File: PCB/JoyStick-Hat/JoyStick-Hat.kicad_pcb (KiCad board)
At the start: 4 copper layers, 65 x 120 mm, 88 parts, among them J1 20021121-00010C4LF, J14 Conn_01x03_Pin, J15 Conn_01x03_Pin, J16 Conn_01x06, J2 BU2032SM-JJ-GTR, J3 Conn_02x05_Odd_Even, J4 Conn_02x04_Odd_Even, J6 1757242, J7 Raspberry_Pi_2_3, J8 Conn_01x04_Pin, J9 Conn_01x04_Pin, M1 D24V22F12, M2 D24V22F5, M3 D24V22F3, SW1 TL3301NF260QG, U1 STM32F446VETx, U4 MAX3535ECWI+T, X1 ABM3B-8.000MHZ-B2-T, X2 ABS07-32.768KHZ-9-T

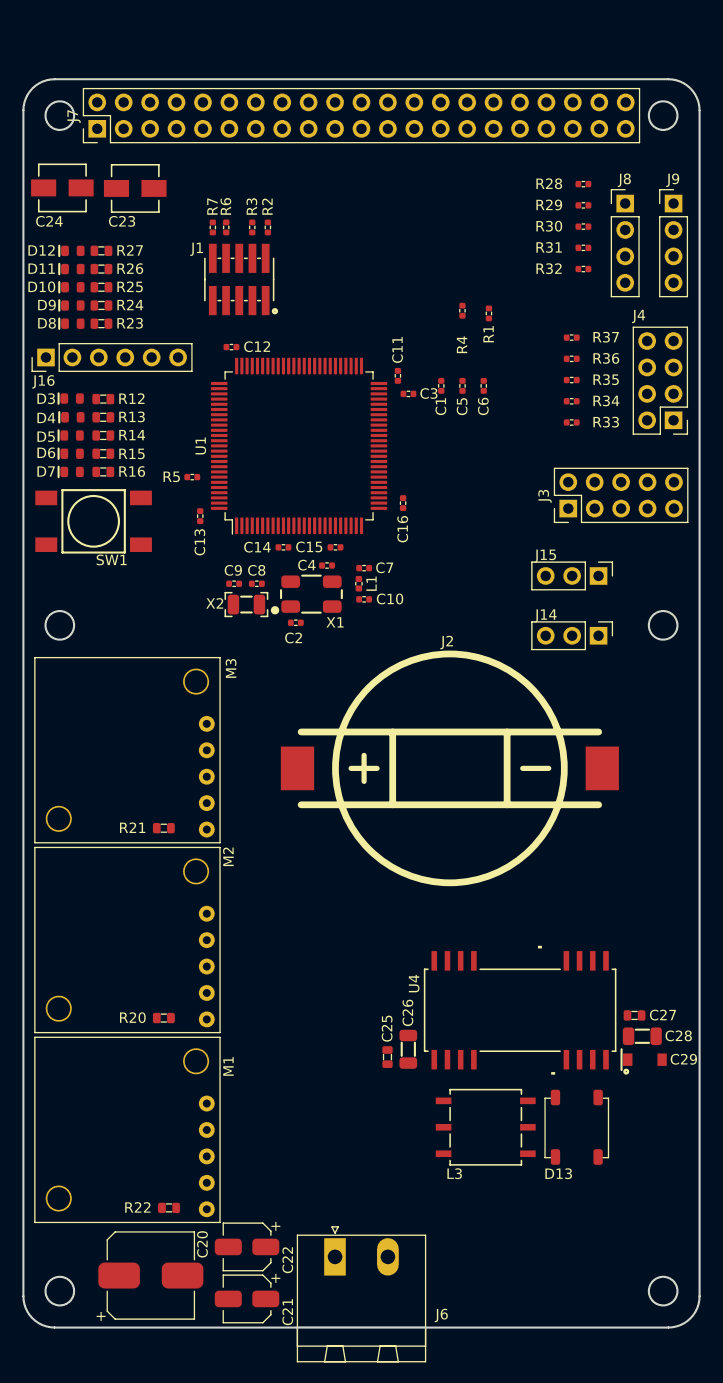
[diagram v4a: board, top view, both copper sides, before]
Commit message: Board Routing
Connectors swapped around and board route started
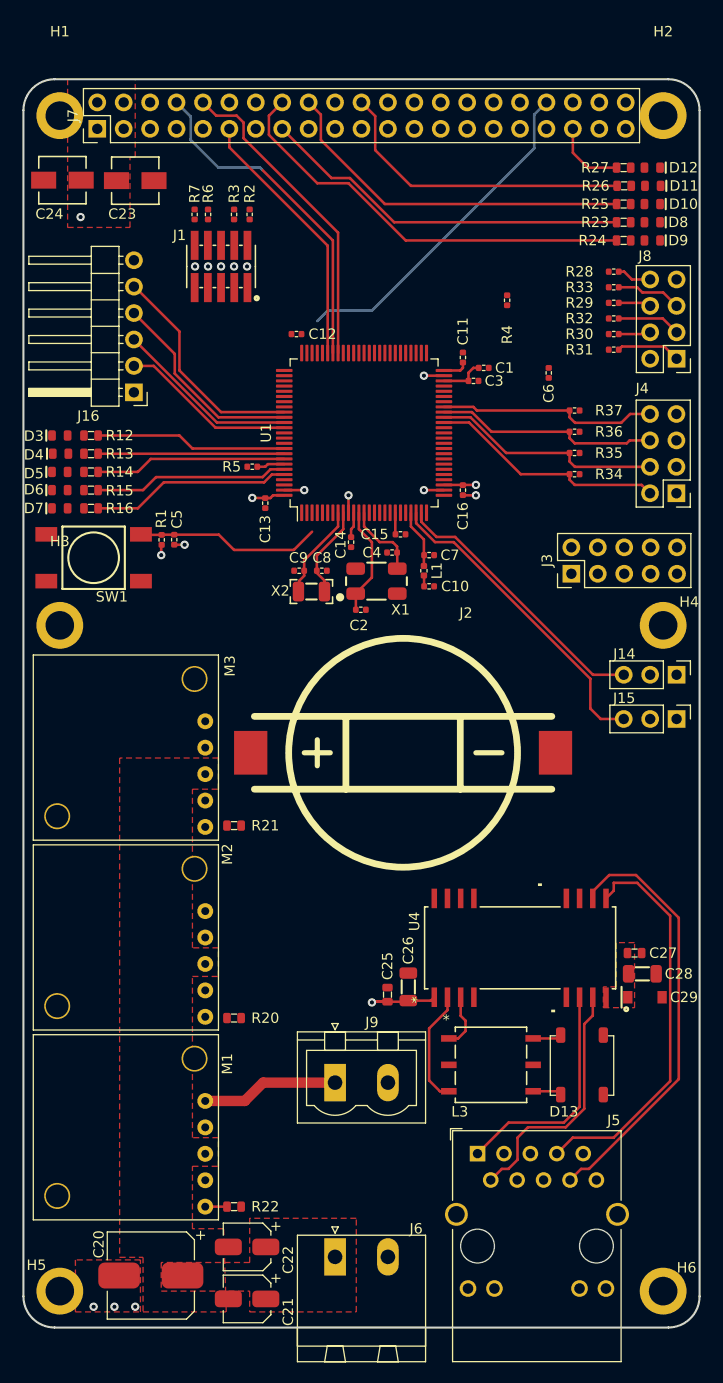
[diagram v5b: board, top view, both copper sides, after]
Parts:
- added H1: MountingHole_Pad, AVR-KiCAD-Lib-Holes_Fasteners:RPI_HAT_HOLE, F.Cu at (203.5, 43.0)
- added H2: MountingHole_Pad, AVR-KiCAD-Lib-Holes_Fasteners:RPI_HAT_HOLE, F.Cu at (261.5, 43.0)
- added H3: MountingHole_Pad, AVR-KiCAD-Lib-Holes_Fasteners:RPI_HAT_HOLE, F.Cu at (203.5, 92.0)
- added H4: MountingHole_Pad, AVR-KiCAD-Lib-Holes_Fasteners:RPI_HAT_HOLE, F.Cu at (261.5, 92.0)
- added H5: MountingHole_Pad, AVR-KiCAD-Lib-Holes_Fasteners:RPI_HAT_HOLE, F.Cu at (203.5, 156.0)
- added H6: MountingHole_Pad, AVR-KiCAD-Lib-Holes_Fasteners:RPI_HAT_HOLE, F.Cu at (261.5, 156.0)
- added J5: 8P8C_LED_Shielded, AVR-KiCAD-Lib-Connectors:RJ45_Wuerth_7499111446_Horizontal, F.Cu at (243.7, 142.8)
- J16: footprint Connector_PinHeader_2.54mm:PinHeader_1x06_P2.54mm_Vertical -> Connector_PinHeader_2.54mm:PinHeader_1x06_P2.54mm_Horizontal
- J8: value Conn_01x04_Pin -> Conn_02x04_Odd_Even; footprint Connector_PinHeader_2.54mm:PinHeader_1x04_P2.54mm_Vertical -> Connector_PinHeader_2.54mm:PinHeader_2x04_P2.54mm_Vertical
- J9: value Conn_01x04_Pin -> 1755736; footprint Connector_PinHeader_2.54mm:PinHeader_1x04_P2.54mm_Vertical -> AVR-KiCAD-Lib-Connectors:PhoenixContact_MSTBVA-G_02x5.08mm_Vertical
- moved J9 90.6 mm to (230.0, 136.0)
- moved D8 56.5 mm to (260.4, 53.2), turned to 0 degrees
- moved D11 56.3 mm to (260.5, 49.8), turned to 0 degrees
- moved D10 56.3 mm to (260.4, 51.5), turned to 0 degrees
- moved D12 56.3 mm to (260.4, 48.0), turned to 0 degrees
- moved D9 56.0 mm to (260.4, 55.0), turned to 0 degrees
- moved R23 51.1 mm to (257.7, 53.2), turned to 180 degrees
- moved R26 50.9 mm to (257.8, 49.8), turned to 180 degrees
- moved R25 50.8 mm to (257.7, 51.5), turned to 180 degrees
- moved R27 50.8 mm to (257.7, 48.0), turned to 180 degrees
- moved R24 50.6 mm to (257.7, 55.0)
- moved R1 38.3 mm to (213.3, 83.8)
- moved C5 31.4 mm to (214.5, 83.8), turned to -90 degrees
- moved J8 15.7 mm to (262.8, 66.4), turned to 180 degrees
- moved J15 15.7 mm to (262.8, 101.0)
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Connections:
- D3 pad 2: unconnected-(D3-Pad2) -> GND
- D4 pad 2: unconnected-(D4-Pad2) -> GND
- D5 pad 2: unconnected-(D5-Pad2) -> GND
- D6 pad 2: unconnected-(D6-Pad2) -> GND
- D7 pad 2: unconnected-(D7-Pad2) -> GND
- J8 pad 2: /JoyStick Interface/ROTARY1_POLE2 -> GND
- J8 pad 3: /JoyStick Interface/ROTARY1_POLE3 -> /JoyStick Interface/ROTARY1_POLE2
- J8 pad 4: GND -> /JoyStick Interface/ROTARY2_POLE3
- J9 pad 1: /JoyStick Interface/ROTARY2_POLE1 -> +12V
- J9 pad 2: /JoyStick Interface/ROTARY2_POLE2 -> GND
- U1 pad 84: Net-(J16-Pin_2) -> Net-(J16-Pin_5)
- U1 pad 85: Net-(J16-Pin_3) -> Net-(J16-Pin_4)
- U1 pad 86: Net-(J16-Pin_4) -> Net-(J16-Pin_3)
- U1 pad 87: Net-(J16-Pin_5) -> Net-(J16-Pin_2)
- U4 pad 12: unconnected-(U4-Z-Pad12) -> Net-(U4-Z)
- U4 pad 13: unconnected-(U4-Y-Pad13) -> Net-(U4-Y)
- U4 pad 15: unconnected-(U4-B-Pad15) -> Net-(U4-B)
- U4 pad 16: unconnected-(U4-A-Pad16) -> Net-(U4-A)
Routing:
- net (no net): track 0.00 -> 355.4 mm
- net +5V: track 0.00 -> 73.8 mm, vias 0 -> 1
- net Net-(U4-A): track 0.00 -> 41.3 mm
- net Net-(J7-GPIO23): track 0.00 -> 41.3 mm
- net Net-(U4-B): track 0.00 -> 38.2 mm
- net Net-(J7-GPIO22): track 0.00 -> 35.9 mm
- net Net-(J7-GPIO24): track 0.00 -> 35.1 mm
- net /RPi_Interface/RPI_ST_UART_TX: track 0.00 -> 32.7 mm
- net /RPi_Interface/RPI_ST_UART_CTS: track 0.00 -> 32.6 mm
- net /RPi_Interface/RPI_ST_UART_RX: track 0.00 -> 30.6 mm
- net /JoyStick Interface/JOYSTICK_Y: track 0.00 -> 30.4 mm
- net Net-(J7-GPIO25): track 0.00 -> 29.8 mm
- net /JoyStick Interface/JOYSTICK_X: track 0.00 -> 26.4 mm
- net /RPi_Interface/RPI_ST_UART_RTS: track 0.00 -> 25.5 mm
- net Net-(U4-Y): track 0.00 -> 24.1 mm
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- added copper zone on F.Cu, net +24V
- added copper zone on In2.Cu, net +3.3V
- added copper zone on F.Cu, net +5V
- added copper zone on F.Cu, net GND
- added copper zone on In1.Cu, net GND
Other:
- outline, holes or cut-outs redrawn

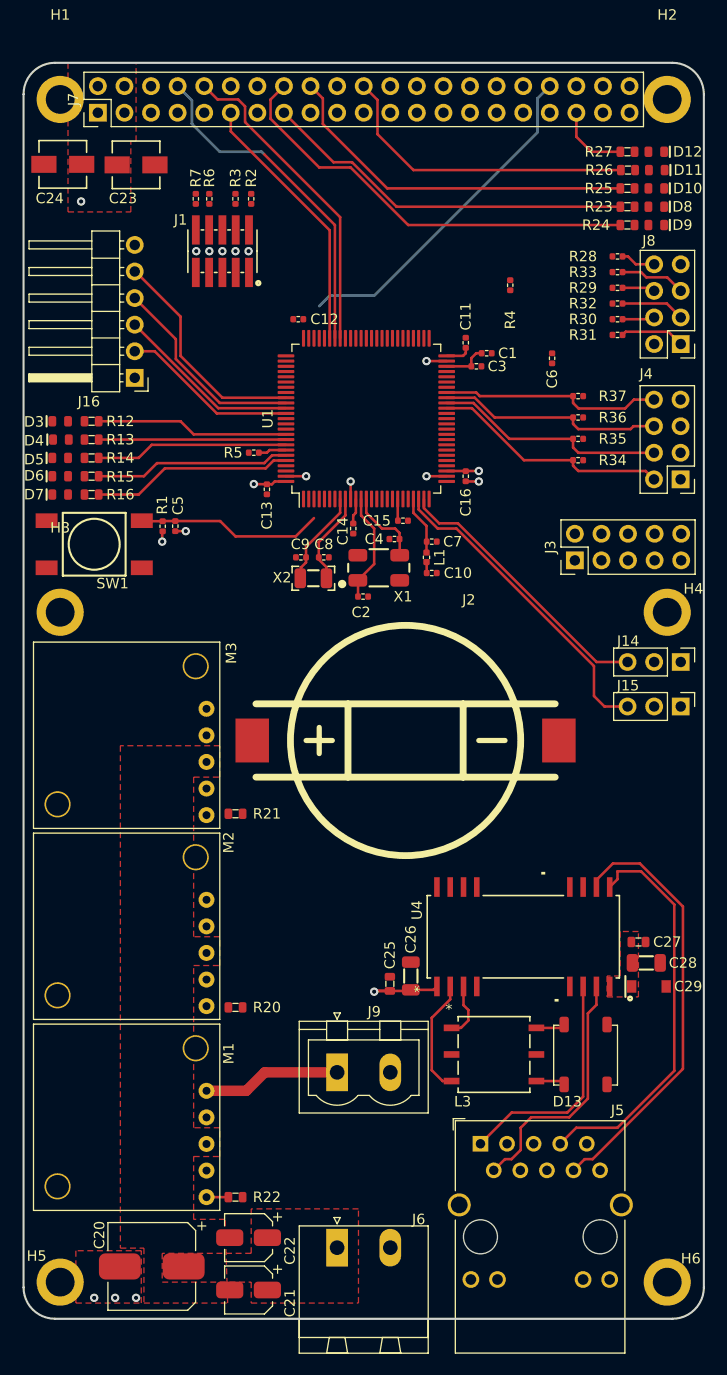
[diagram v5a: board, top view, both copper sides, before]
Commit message: Board Progress
Board route nearly complete, internal power plane topologys witched up to run 5Vs as plane. Reset buttom moved. Next: add more LEDs and breakout more STM32 pins for development purposes.
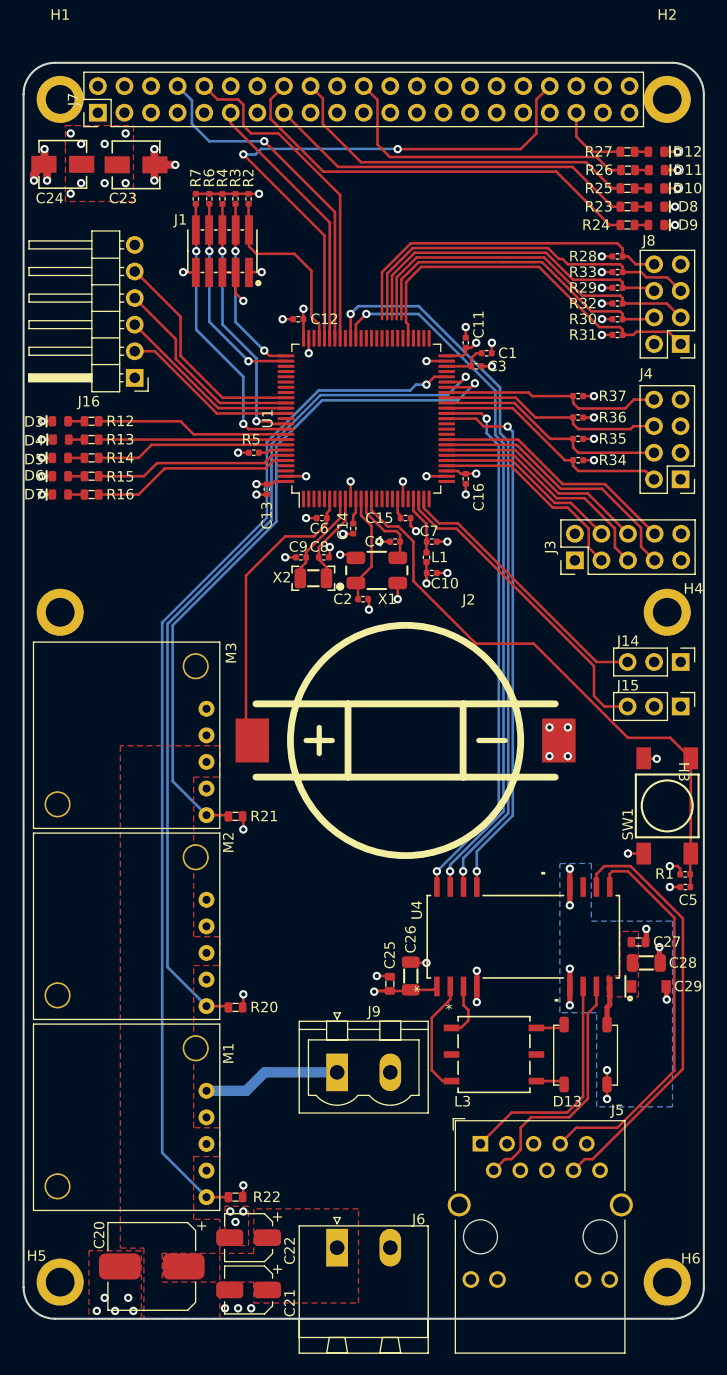
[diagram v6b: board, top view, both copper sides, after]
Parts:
- moved SW1 60.2 mm to (261.5, 110.5), turned to -90 degrees
- moved R1 60.0 mm to (263.2, 117.0), turned to 0 degrees
- moved C5 59.7 mm to (263.2, 118.2), turned to 180 degrees
- moved R4 28.7 mm to (219.0, 52.5), turned to -90 degrees
- moved C6 26.8 mm to (228.5, 83.0), turned to 180 degrees
- moved C15 0.35 mm to (236.5, 83.0)
- moved X1 0.31 mm to (233.8, 88.0)
- moved C4 0.26 mm to (235.5, 85.2)
- moved C16 0.25 mm to (242.2, 79.2)
- moved C2 0.25 mm to (232.4, 90.8)
- moved R2 0.25 mm to (221.5, 52.5)
- moved R21 0.25 mm to (220.2, 111.5), turned to 0 degrees
- turned R20 to 0 degrees
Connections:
- C10 pad 1: +3V3 -> +3.3V
- C11 pad 1: +3V3 -> +3.3V
- C12 pad 1: +3V3 -> +3.3V
- C13 pad 1: +3V3 -> +3.3V
- C14 pad 1: +3V3 -> +3.3V
- C15 pad 1: +3V3 -> +3.3V
- C16 pad 1: +3V3 -> +3.3V
- J1 pad 1: +3V3 -> +3.3V
- J3 pad 1: +3V3 -> +3.3V
- J3 pad 2: +3V3 -> +3.3V
- J3 pad 3: /STM32F446RET6-MCU/LED_DRIVER_SCLK -> /STM32F446RET6-MCU/LED_DRIVER_XLAT
- J3 pad 4: /STM32F446RET6-MCU/LED_DRIVER_XLAT -> /STM32F446RET6-MCU/LED_DRIVER_SCLK
- J3 pad 6: /STM32F446RET6-MCU/LED_DRIVER_BLANK -> /STM32F446RET6-MCU/LED_DRIVER_MOSI
- J3 pad 7: /STM32F446RET6-MCU/LED_DRIVER_MOSI -> /STM32F446RET6-MCU/LED_DRIVER_BLANK
- L1 pad 1: +3V3 -> +3.3V
- R1 pad 1: +3V3 -> +3.3V
- R2 pad 1: +3V3 -> +3.3V
- R3 pad 1: +3V3 -> +3.3V
- R4 pad 1: +3V3 -> +3.3V
- R6 pad 1: +3V3 -> +3.3V
- R7 pad 1: +3V3 -> +3.3V
- U1 pad 100: +3V3 -> +3.3V
- U1 pad 11: +3V3 -> +3.3V
- U1 pad 19: +3V3 -> +3.3V
- U1 pad 28: +3V3 -> +3.3V
- U1 pad 50: +3V3 -> +3.3V
- U1 pad 75: +3V3 -> +3.3V
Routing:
- net GND: track 9.71 -> 422.3 mm, vias 9 -> 64
- net (no net): track 355.4 -> 0.00 mm
- net /Power/12V_PG: track 2.09 -> 99.9 mm, vias 0 -> 1
- net /Power/5V_PG: track 0.00 -> 84.7 mm, vias 0 -> 1
- net +5V: track 73.8 -> 3.75 mm, vias 1 -> 8
- net /RS485 To Motor Controller Interface/RS485_RX_EN: track 0.00 -> 70.0 mm, vias 0 -> 2
- net /RS485 To Motor Controller Interface/RS485_TX_EN: track 0.00 -> 68.0 mm, vias 0 -> 2
- net /Power/3.3V_PG: track 0.00 -> 67.2 mm, vias 0 -> 1
- net /RS485 To Motor Controller Interface/RS485_TXD: track 0.00 -> 51.8 mm, vias 0 -> 2
- net /RS485 To Motor Controller Interface/RS485_RXD: track 0.00 -> 51.7 mm, vias 0 -> 2
- net +3.3V: track 7.63 -> 51.0 mm, vias 1 -> 22
- net /STM32F446RET6-MCU/NRST: track 17.8 -> 55.9 mm
- net /JoyStick Interface/ROTARY1_POLE1: track 6.17 -> 35.9 mm
- net /JoyStick Interface/ROTARY2_POLE1: track 3.33 -> 32.9 mm
- net /JoyStick Interface/ROTARY1_POLE3: track 6.30 -> 35.4 mm
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- added copper zone on In2.Cu, net +5V
- added copper zone on B.Cu, net Earth

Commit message: PCB First Pass Complete
First complete pass at PCB finished. Added more debug LEDs for both STM32 and RPi, 8 totaly so binary data can be outputted as a byte etc, that way we can have debug codes. Added heartbeat LED to STM32. Rearranged connectors and pinning of certain connectors to make routing smooth and traces short.
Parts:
- removed J16: Conn_01x06, Connector_PinHeader_2.54mm:PinHeader_1x06_P2.54mm_Horizontal
- added D1: LTST-C194TBKT, AVR-KiCAD-Lib-Diodes:LED0603, F.Cu at (204.2, 86.0)
- added D14: LTST-C194TBKT, AVR-KiCAD-Lib-Diodes:LED0603, F.Cu at (204.2, 77.0)
- added D15: LTST-C194KGKT, AVR-KiCAD-Lib-Diodes:LED0603, F.Cu at (260.5, 51.2)
- added D16: LTST-C194KGKT, AVR-KiCAD-Lib-Diodes:LED0603, F.Cu at (260.5, 49.8)
- added D17: LTST-C194KGKT, AVR-KiCAD-Lib-Diodes:LED0603, F.Cu at (260.5, 48.2)
- added D18: LTST-C194TBKT, AVR-KiCAD-Lib-Diodes:LED0603, F.Cu at (244.0, 90.5)
- added D2: LTST-C194TBKT, AVR-KiCAD-Lib-Diodes:LED0603, F.Cu at (204.2, 87.5)
- added J10: Conn_02x06_Odd_Even, Connector_PinHeader_2.54mm:PinHeader_2x06_P2.54mm_Horizontal, F.Cu at (212.7, 70.1)
- added R10: RC0603FR-07470RL, AVR-KiCAD-Lib-Resistors:R0603, F.Cu at (207.2, 77.0)
- added R11: RC0603FR-07470RL, AVR-KiCAD-Lib-Resistors:R0603, F.Cu at (257.8, 51.2)
- added R17: RC0603FR-07470RL, AVR-KiCAD-Lib-Resistors:R0603, F.Cu at (257.8, 49.8)
- added R18: RC0603FR-07470RL, AVR-KiCAD-Lib-Resistors:R0603, F.Cu at (257.8, 48.2)
- added R19: RC0603FR-07470RL, AVR-KiCAD-Lib-Resistors:R0603, F.Cu at (244.0, 87.7)
- added R8: RC0603FR-07470RL, AVR-KiCAD-Lib-Resistors:R0603, F.Cu at (207.2, 86.0)
- added R9: RC0603FR-07470RL, AVR-KiCAD-Lib-Resistors:R0603, F.Cu at (207.2, 87.5)
- moved D3 4.81 mm to (204.2, 78.5)
- moved R12 4.81 mm to (207.2, 78.5)
- moved D4 4.56 mm to (204.3, 80.0)
- moved R13 4.56 mm to (207.2, 80.0)
- moved D5 4.32 mm to (204.2, 81.5)
- moved R14 4.32 mm to (207.2, 81.5)
- moved D6 4.07 mm to (204.2, 83.0)
- moved R15 4.07 mm to (207.2, 83.0)
- moved D7 3.82 mm to (204.2, 84.5)
- moved R16 3.82 mm to (207.2, 84.5)
- moved J1 3.25 mm to (222.2, 57.5)
- moved R2 3.25 mm to (224.8, 52.5)
- moved R3 3.25 mm to (223.5, 52.5)
- moved R4 3.25 mm to (222.2, 52.5)
- moved R6 3.25 mm to (221.0, 52.5)
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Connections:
- J7 pad 33: unconnected-(J7-PWM1/GPIO13-Pad33) -> Net-(J7-PWM1/GPIO13)
- J7 pad 35: unconnected-(J7-GPIO19/MISO1-Pad35) -> Net-(J7-GPIO19/MISO1)
- J7 pad 38: unconnected-(J7-GPIO20/MOSI1-Pad38) -> Net-(J7-GPIO20/MOSI1)
- U1 pad 25: unconnected-(U1-PA2-Pad25) -> Net-(U1-PA2)
- U1 pad 56: /JoyStick Interface/ROTARY1_POLE2 -> /JoyStick Interface/ROTARY2_POLE3
- U1 pad 57: /JoyStick Interface/ROTARY1_POLE3 -> /JoyStick Interface/ROTARY1_POLE2
- U1 pad 58: /JoyStick Interface/ROTARY2_POLE1 -> /JoyStick Interface/ROTARY2_POLE2
- U1 pad 59: /JoyStick Interface/ROTARY2_POLE2 -> /JoyStick Interface/ROTARY1_POLE3
- U1 pad 60: /JoyStick Interface/ROTARY2_POLE3 -> /JoyStick Interface/ROTARY2_POLE1
- U1 pad 78: unconnected-(U1-PC10-Pad78) -> /STM32F446RET6-MCU/PC10
- U1 pad 79: unconnected-(U1-PC11-Pad79) -> /STM32F446RET6-MCU/PC11
- U1 pad 80: unconnected-(U1-PC12-Pad80) -> /STM32F446RET6-MCU/PC12
- U1 pad 81: unconnected-(U1-PD0-Pad81) -> /STM32F446RET6-MCU/PD0
- U1 pad 82: unconnected-(U1-PD1-Pad82) -> /STM32F446RET6-MCU/PD1
- U1 pad 83: unconnected-(U1-PD2-Pad83) -> /STM32F446RET6-MCU/PD2
- U1 pad 84: Net-(J16-Pin_5) -> /STM32F446RET6-MCU/PD3
- U1 pad 85: Net-(J16-Pin_4) -> /STM32F446RET6-MCU/PD4
- U1 pad 86: Net-(J16-Pin_3) -> /STM32F446RET6-MCU/PD5
- U1 pad 87: Net-(J16-Pin_2) -> /STM32F446RET6-MCU/PD6
- U1 pad 88: unconnected-(U1-PD7-Pad88) -> Net-(U1-PD7)
- U1 pad 97: unconnected-(U1-PE0-Pad97) -> Net-(U1-PE0)
- U1 pad 98: unconnected-(U1-PE1-Pad98) -> Net-(U1-PE1)
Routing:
- net +5V: track 3.75 -> 46.8 mm, vias 8 -> 9
- net Net-(J16-Pin_5): track 21.6 -> 0.00 mm
- net /STM32F446RET6-MCU/PC11: track 0.00 -> 21.5 mm
- net Net-(U1-PE1): track 0.00 -> 20.9 mm
- net Net-(U1-PE0): track 0.00 -> 20.5 mm
- net /STM32F446RET6-MCU/PD0: track 0.00 -> 20.4 mm
- net Net-(J16-Pin_4): track 19.7 -> 0.00 mm
- net /STM32F446RET6-MCU/PC10: track 0.00 -> 19.1 mm
- net Net-(U1-PD7): track 0.00 -> 19.0 mm
- net /STM32F446RET6-MCU/PD2: track 0.00 -> 18.5 mm
- net /STM32F446RET6-MCU/PD4: track 0.00 -> 17.9 mm
- net Net-(J16-Pin_3): track 17.8 -> 0.00 mm
- net /STM32F446RET6-MCU/PC12: track 0.00 -> 17.7 mm
- net /STM32F446RET6-MCU/PD6: track 0.00 -> 17.2 mm
- net Net-(J16-Pin_2): track 16.9 -> 0.00 mm
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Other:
- board text added: "12V DCDC"
- board text added: "12V OUT"
- board text added: "24V IN"
- board text added: "3.3V DCDC"
- board text added: "5V DCDC"
- board text added: "ARM Debug"
- board text added: "BTTN"
- board text added: "Debug LED Byte"
- board text added: "Debug LED Pi"
- board text added: "JOYSTICK"
- board text added: "LED DRV"
- board text added: "RESET"
- board text added: "ROTARY"
- board text added: "RS485"
- board text added: "ST HEARTBEAT"
- board text added: "STM32 Debug"
